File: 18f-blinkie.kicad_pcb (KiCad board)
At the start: 2 copper layers, 69.8 x 61.2 mm, 15 parts, among them J1 Conn_01x07_Female, J2 Conn_01x07_Female

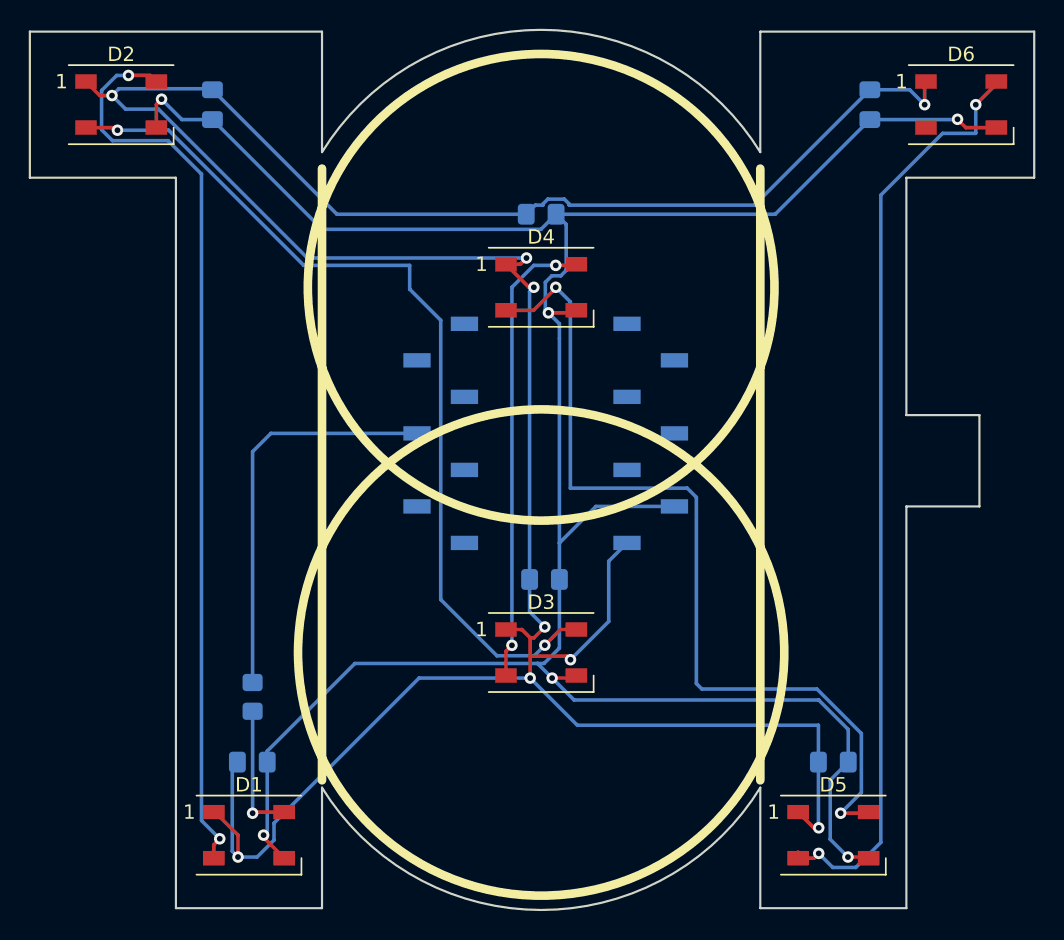
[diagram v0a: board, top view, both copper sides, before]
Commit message: Adding fill. Fixing text.
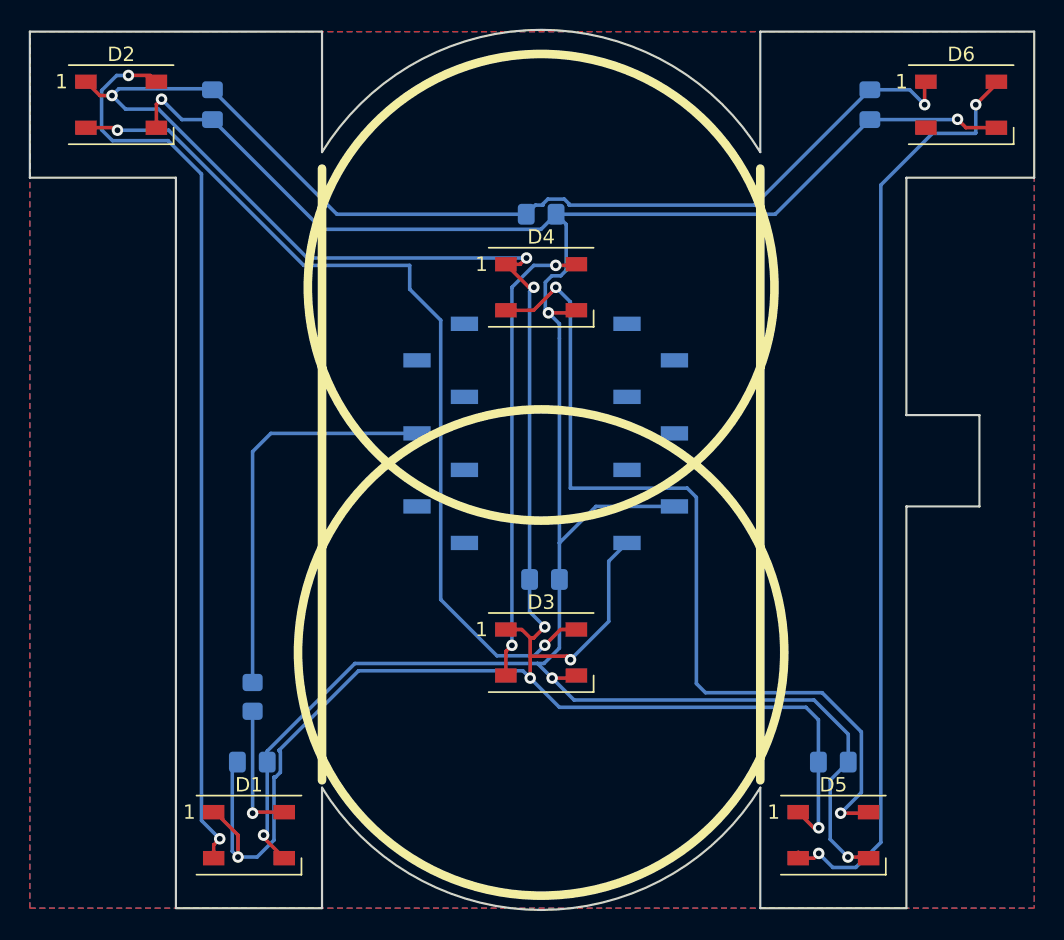
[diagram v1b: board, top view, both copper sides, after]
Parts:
- added REF**: OSHW-Logo2_14.6x12mm_SilkScreen, Symbol:OSHW-Logo2_14.6x12mm_SilkScreen, B.Cu at (88.9, 149.9)
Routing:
- net 5V: track 216.6 -> 220.2 mm
- added copper zone on B.Cu, net (none)
- added copper zone on F.Cu, net (none)
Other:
- board text added: "https://github.com/jadudm/18f-blinkie"
